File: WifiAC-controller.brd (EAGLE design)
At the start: 59.7 x 55.9 mm, 11 parts

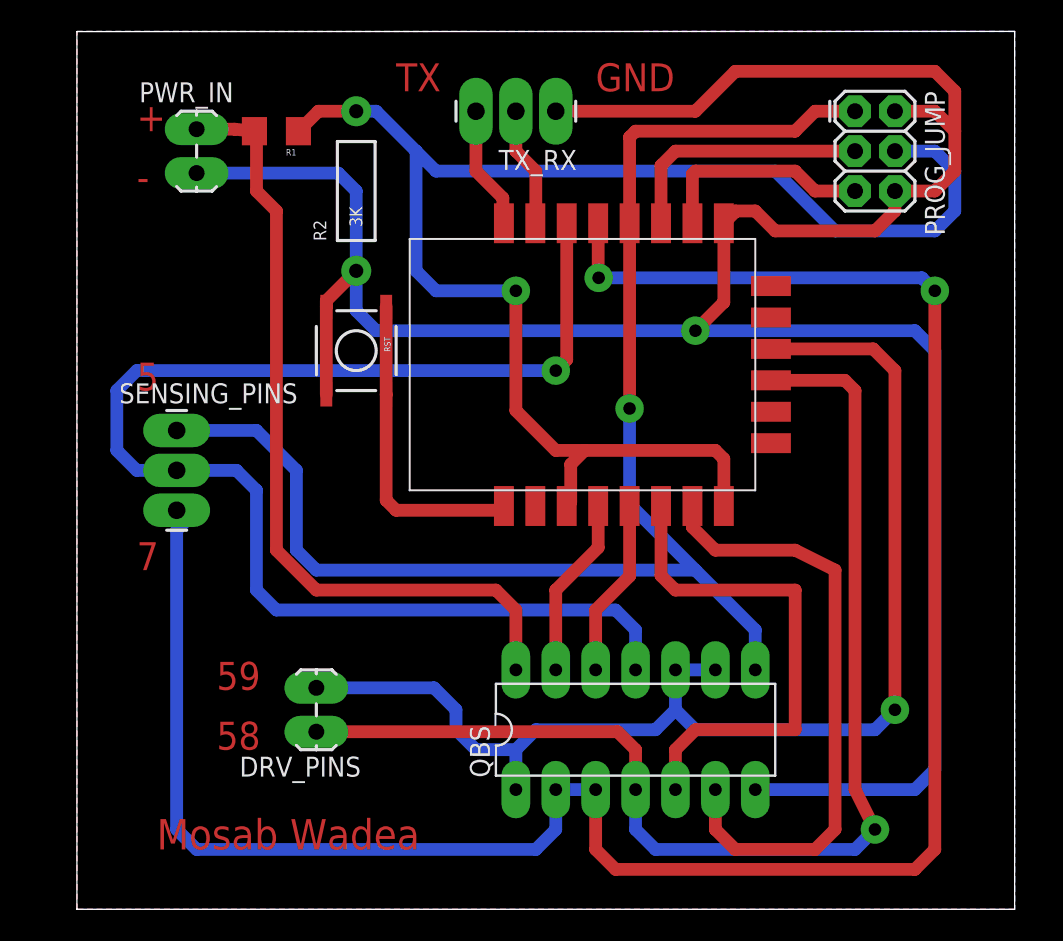
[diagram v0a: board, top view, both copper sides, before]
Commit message: major fixes, changed the esp foot print, changed the connections, changed power supply, made the layout smaller
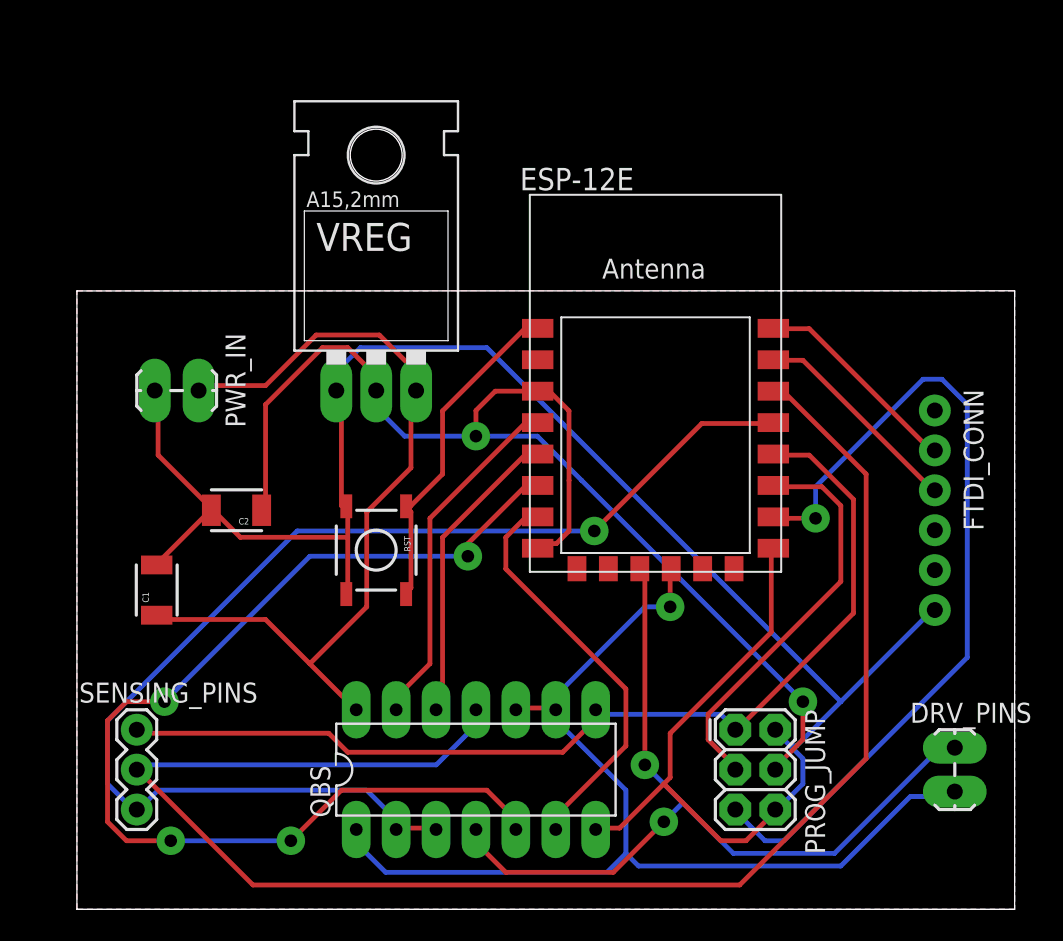
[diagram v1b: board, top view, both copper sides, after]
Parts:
- removed R1: 1.5K, SparkFun-Resistors:1206
- removed R2: 3K, SparkFun-Resistors:AXIAL-0.4
- removed TX_RX: UART, SparkFun-Connectors:1X03_LONGPADS
- removed U$1: (no value), WifiAC-controller~~~ref_tmp:_REFERENCE_HOLE_
- added C1: 0.47u, SparkFun-Passives:1210
- added C2: 33u, SparkFun-Passives:1210
- added FTDI_CONN: (no value), SparkFun-Connectors:1X06_NO_SILK
- added VREG: V_REG_LD1117VXX, SparkFun-PowerIC:78XXL
- ESP-12E: value ESP-07/12_ESP-12E -> ESP-07/12; device ESP-12E:ESP-07/12 -> ESP-12E:ESP-12E
- SENSING_PINS: device SparkFun-Connectors:1X03_LONGPADS -> SparkFun-Connectors:1X03
- moved DRV_PINS 40.7 mm to (55.9, 10.2), turned to 270 degrees
- moved PROG_JUMP 40.1 mm to (41.9, 11.4)
- moved SENSING_PINS 19.2 mm to (3.81, 11.4)
- moved PWR_IN 16.5 mm to (7.62, 33.0), turned to 180 degrees
- moved RST 12.8 mm to (19.1, 22.9)
- moved QBS_ 10.5 mm to (25.4, 8.89)
- moved ESP-12E 7.41 mm to (36.8, 30.5), turned to 0 degrees
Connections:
- removed net N$3: ESP-12E.TXD0, TX_RX.3
- removed net N$4: ESP-12E.RXD0, TX_RX.2
- new net RX: ESP-12E.16, FTDI_CONN.2
- new net TX: ESP-12E.15, FTDI_CONN.3
- net 3V3: now also C2.1, ESP-12E.3, ESP-12E.8, VREG.GND; no longer ESP-12E.EN, ESP-12E.VCC, R1.1, R2.P$2
- net 5V: now also C1.1, VREG.OUT; no longer R1.2
- net GND: now also C1.2, C2.2, ESP-12E.9, FTDI_CONN.6, VREG.IN; no longer ESP-12E.GND, R2.P$1, TX_RX.1
- net GPIO12: now also ESP-12E.6; no longer ESP-12E.GPIO12
- net GPIO13: now also ESP-12E.7; no longer ESP-12E.GPIO13
- net GPIO14: now also ESP-12E.5; no longer ESP-12E.GPIO14
- net GPIO15: now also ESP-12E.10; no longer ESP-12E.GPIO15
- net GPIO16: now also ESP-12E.4; no longer ESP-12E.GPIO16
- net GPIO2: now also ESP-12E.11; no longer ESP-12E.GPIO2
- net N$1: now also ESP-12E.1; no longer ESP-12E.REST
- net P5: now also ESP-12E.12; no longer ESP-12E.GPIO0
- net P58: now also ESP-12E.19; no longer ESP-12E.GPIO9
- net P59: now also ESP-12E.20; no longer ESP-12E.GPIO10
- net P6: now also ESP-12E.14; no longer ESP-12E.GPIO5
- net P7: now also ESP-12E.13; no longer ESP-12E.GPIO4
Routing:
- net P7: track 139.6 -> 77.9 mm, vias 2 -> 1
- net GPIO15: track 14.1 -> 54.4 mm, vias 0 -> 1
- net GPIO12: track 32.9 -> 69.8 mm, vias 0 -> 4
- net GND: track 165.3 -> 132.5 mm, vias 1 -> 0
- net P5: track 91.9 -> 65.1 mm, vias 1 -> 0
- net P58: track 76.0 -> 54.4 mm, vias 1 -> 2
- net 3V3: track 96.6 -> 77.0 mm, vias 1 -> 2
- net P6: track 86.0 -> 102.8 mm, vias 1 -> 0
- net TX: track 0.00 -> 13.7 mm
- net RX: track 0.00 -> 13.5 mm
- net GPIO13: track 39.1 -> 26.2 mm
- net GPIO16: track 11.5 -> 22.5 mm
- net GPIO2: track 16.4 -> 25.8 mm
- net P59: track 79.0 -> 69.6 mm
- net GPIO14: track 11.3 -> 19.4 mm
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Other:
- board size 59.7 x 55.9 mm -> 59.7 x 39.4 mm
- board text removed: "+"
- board text removed: "-"
- board text removed: "5"
- board text removed: "58"
- board text removed: "59"
- board text removed: "7"
- board text removed: "GND"
- board text removed: "Mosab Wadea"
- board text removed: "TX"

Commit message: generated new mill path and cutting pref
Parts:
- added _REFERENCE_HOLE_: (no value), WifiAC-controller~~~ref_tmp:_REFERENCE_HOLE_

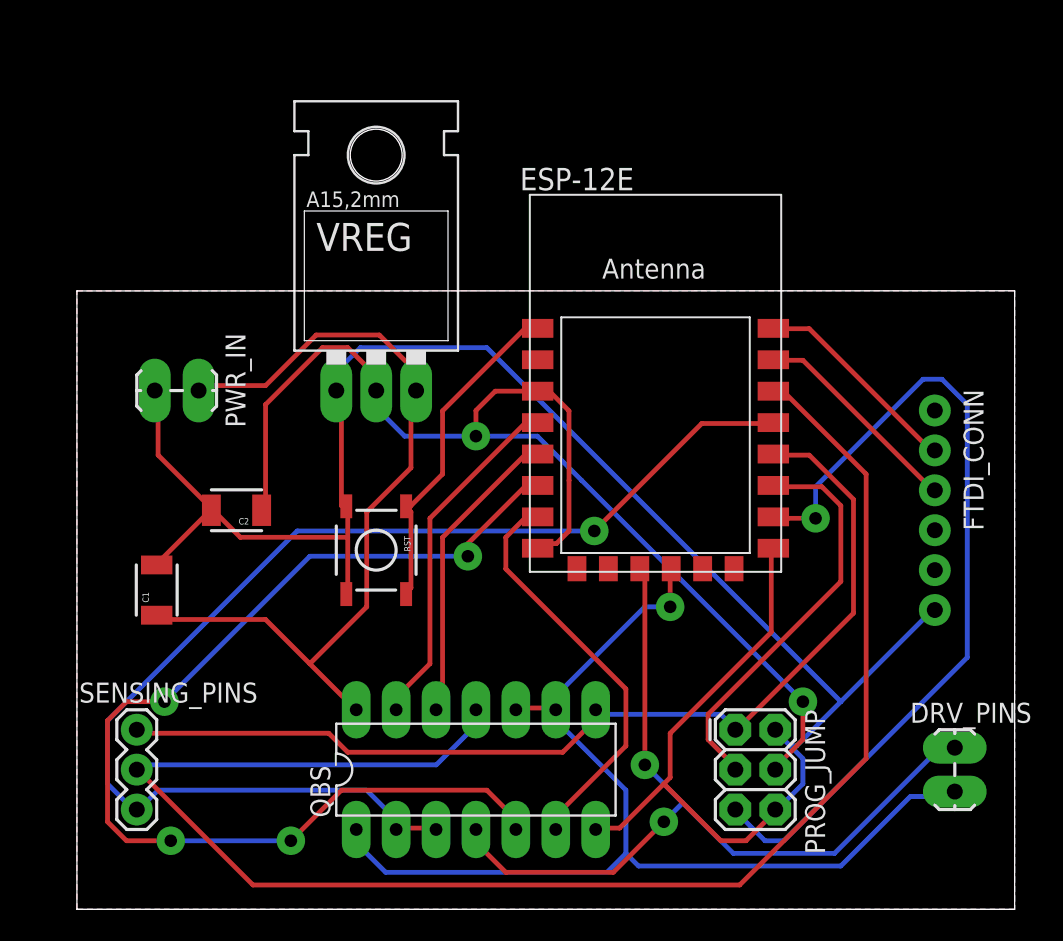
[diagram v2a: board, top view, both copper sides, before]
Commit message: changed the smd capacitors to through hole
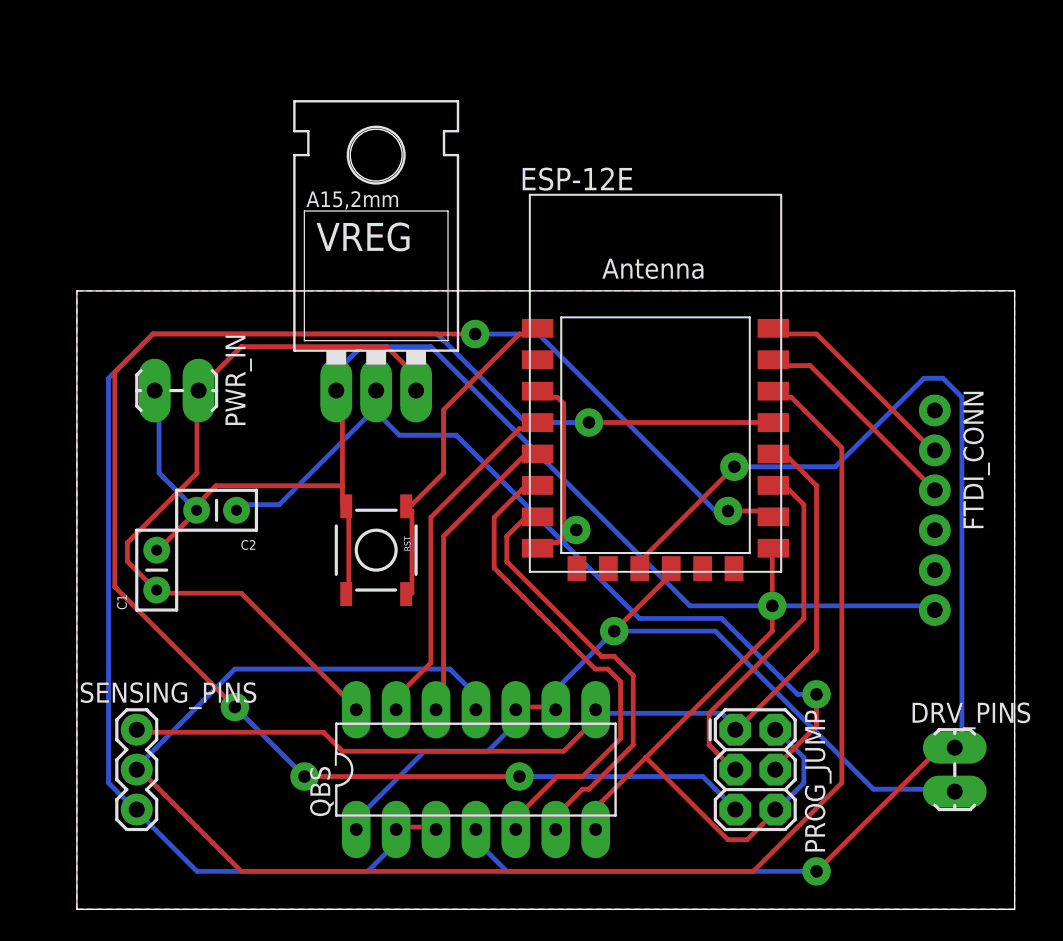
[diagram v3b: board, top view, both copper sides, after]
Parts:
- C1: device SparkFun-Passives:1210 -> SparkFun-Passives:CAP-PTH-SMALLEZ
- C2: device SparkFun-Passives:1210 -> SparkFun-Passives:CAP-PTH-SMALL2
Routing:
- net GPIO15: track 54.4 -> 107.0 mm, vias 1 -> 5
- net GPIO12: track 69.8 -> 31.0 mm, vias 4 -> 0
- net P58: track 54.4 -> 84.2 mm
- net P7: track 77.9 -> 96.4 mm
- net P59: track 69.6 -> 54.8 mm
- net GND: track 132.5 -> 123.8 mm, vias 0 -> 1
- net 3V3: track 77.0 -> 70.2 mm
- net 5V: track 53.1 -> 48.0 mm
- net GPIO2: track 25.8 -> 22.6 mm
- net P5: track 65.1 -> 62.4 mm
- net GPIO13: track 26.2 -> 27.2 mm
- added copper zone on layer 1, net N$2
- removed copper zone on layer 1, net GND
